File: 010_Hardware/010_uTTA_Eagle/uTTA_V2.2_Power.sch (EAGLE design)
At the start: 124 parts, among them IC1 MCP14E09, IC101 78L05SMD, IC102 7905ACM, IC103 LM393D, IC105 LT1167, IC2 SFH6156, IC3 SFH6156, IC4 SFH6156, J102 PIN23866A.68, J103 PIN23866A.68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

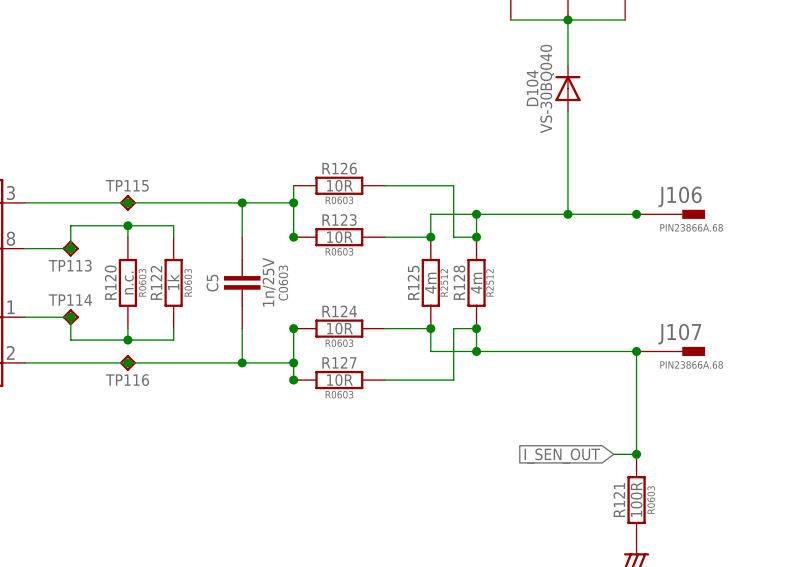
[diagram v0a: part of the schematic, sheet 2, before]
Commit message: Update to uTTA Version 2.2
Full update of both PCBs to HW Version 2.2:
Removed spare FLASH Memory
Adjusted Position of LEDs and Buttons
Cleanup of layout
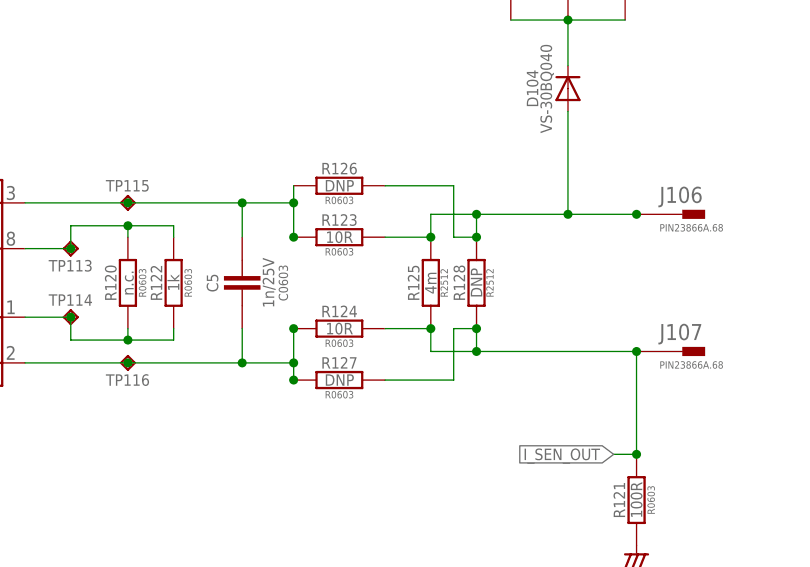
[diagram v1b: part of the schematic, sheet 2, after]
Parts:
- R126, R127: value 10R -> DNP
- R128: value 4m -> DNP
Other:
- note added: "2mv/A Ptot @ 15A: 0.9W"
- note added: "AV = 50V/V 15A -> 3.0V ~4.02mA/digit"
- note added: "AV = 50V/V 15A -> 3.0V ~4.02mA/digit tau = 2.2µs fc = 72.343kHz"
- note removed: "2mv/A Ptot @ 30A: 1.8W"
- note removed: "AV = 50V/V 30A -> 1.5V ~12.2mA/digit"
- note removed: "AV = 50V/V 30A -> 1.5V ~12.2mA/digit tau = 2.2µs fc = 72.343kHz"
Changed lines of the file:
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@@
 <schematic xreflabel="%F%N/%S.%C%R" xrefpart="/%S.%C%R">
 <attributes>
-<attribute name="VERSION" value="V1.0"/>
+<attribute name="VERSION" value="2.2"/>
 </attributes>
 <variantdefs>
@@
 </classes>
 <parts>
-<part name="R127" library="A_Resistor" deviceset="R-EU_" device="R0603" value="10R"/>
+<part name="R127" library="A_Resistor" deviceset="R-EU_" device="R0603" value="DNP"/>
 <part name="R124" library="A_Resistor" deviceset="R-EU_" device="R0603" value="10R"/>
 <part name="R123" library="A_Resistor" deviceset="R-EU_" device="R0603" value="10R"/>
-<part name="R126" library="A_Resistor" deviceset="R-EU_" device="R0603" value="10R"/>
+<part name="R126" library="A_Resistor" deviceset="R-EU_" device="R0603" value="DNP"/>
 <part name="R118" library="A_Resistor" deviceset="R-EU_" device="R0603" value="10R">
 <attribute name="PACKAGE" value="R0603"/>
@@
 <part name="D101" library="A_Dioden" deviceset="DIODE-" device="SOD123" value="1N4148"/>
 <part name="D102" library="A_Dioden" deviceset="DIODE-" device="SOD123" value="1N4148"/>
-<part name="R128" library="A_Shunts" deviceset="WSL2512" device="" value="4m"/>
+<part name="R128" library="A_Shunts" deviceset="WSL2512" device="" value="DNP"/>
 <part name="R125" library="A_Shunts" deviceset="WSL2512" device="" value="4m"/>
 <part name="C101" library="A_Kondensatoren" deviceset="CPOL-EU" device="D" value="47µF/25V"/>
@@
 <text x="144.78" y="152.4" size="2.1844" layer="98">RDS,on ~3.3mR</text>
 <text x="208.28" y="68.58" size="2.1844" layer="98">2mv/A
-Ptot @ 30A: 1.8W</text>
+Ptot @ 15A: 0.9W</text>
 <text x="120.015" y="48.26" size="1.4224" layer="98">AV = 50V/V
-30A -&gt; 1.5V
-~12.2mA/digit</text>
+15A -&gt; 3.0V
+~4.02mA/digit</text>
 <text x="116.205" y="85.725" size="1.27" layer="98">Replaceable with INA128</text>
 <text x="40.64" y="115.57" size="1.27" layer="98">UF=1.7V @ 16mA</text>
 <text x="97.155" y="53.34" size="1.4224" layer="98">AV = 50V/V
-30A -&gt; 1.5V
-~12.2mA/digit
+15A -&gt; 3.0V
+~4.02mA/digit
 tau = 2.2µs
 fc = 72.343kHz</text>

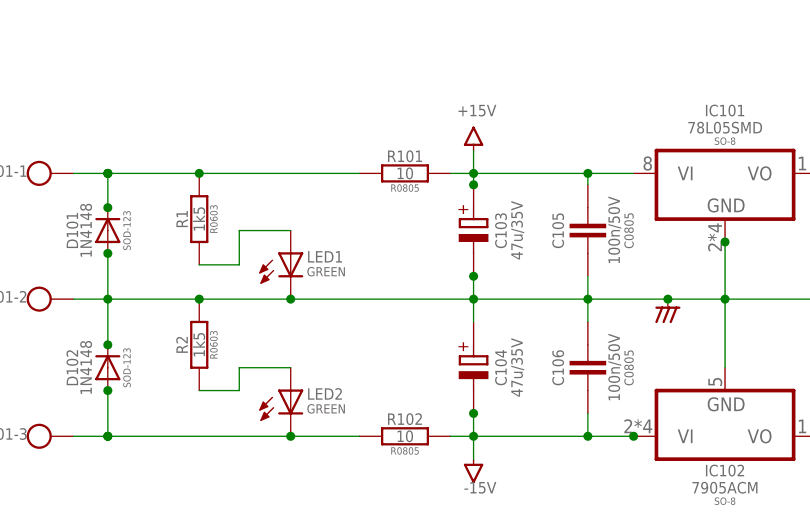
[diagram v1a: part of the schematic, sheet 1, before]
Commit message: changed resistor values
Changed Values of R101 and R102 to 0 Ohm
Changed value of R108 from 100 Ohm to 240 Ohm (to reduce optocoupler LED current)
Changed value of R110 from 220 Ohm to 470 Ohm (to reduce LED current)
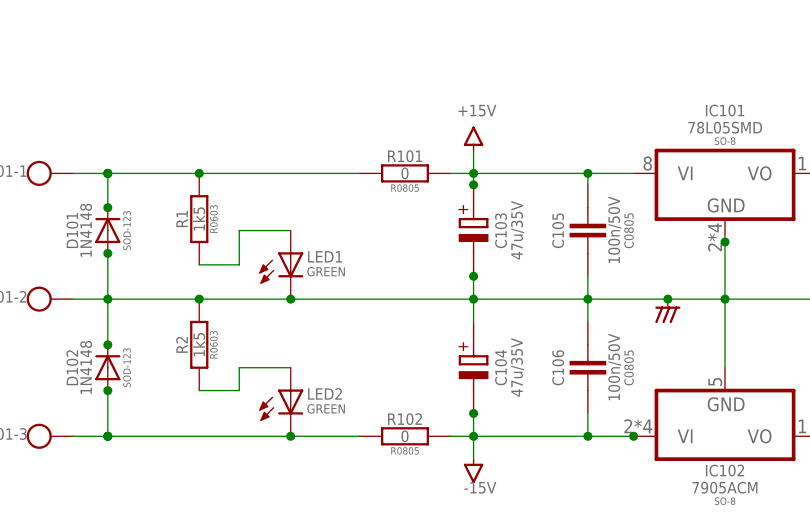
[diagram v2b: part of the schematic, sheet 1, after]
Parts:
- R101, R102: value 10 -> 0
- R108: value 100R -> 240R
- R110: value 270R -> 470R
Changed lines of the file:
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@@
 <schematic xreflabel="%F%N/%S.%C%R" xrefpart="/%S.%C%R">
 <attributes>
-<attribute name="VERSION" value="2.2"/>
+<attribute name="VERSION" value="2.5.3"/>
 </attributes>
 <variantdefs>
@@
 <attribute name="PACKAGE" value="R0603"/>
 </part>
-<part name="R101" library="A_Resistor" deviceset="R-EU_" device="R0805" value="10"/>
-<part name="R102" library="A_Resistor" deviceset="R-EU_" device="R0805" value="10"/>
+<part name="R101" library="A_Resistor" deviceset="R-EU_" device="R0805" value="0"/>
+<part name="R102" library="A_Resistor" deviceset="R-EU_" device="R0805" value="0"/>
 <part name="V40" library="supply" deviceset="+15V" device=""/>
 <part name="V41" library="supply" deviceset="-15V" device=""/>
@@
 <part name="R104" library="A_Resistor" deviceset="R-EU_" device="R0603" value="22k"/>
 <part name="AGND22" library="supply" deviceset="AGND_" device=""/>
-<part name="R108" library="A_Resistor" deviceset="R-EU_" device="R0603" value="100R"/>
+<part name="R108" library="A_Resistor" deviceset="R-EU_" device="R0603" value="240R"/>
 <part name="V2" library="supply" deviceset="GND_ISO" device=""/>
 <part name="AGND23" library="supply" deviceset="AGND_" device=""/>
 <part name="T102" library="A_Transistoren" deviceset="PDTC*" device="" technology="143E"/>
-<part name="R110" library="A_Resistor" deviceset="R-EU_" device="R0603" value="270R"/>
+<part name="R110" library="A_Resistor" deviceset="R-EU_" device="R0603" value="470R"/>
 <part name="TP101" library="A_Testpoint" deviceset="TP" device="C90H30" value="TPC90H30"/>
 <part name="TP104" library="A_Testpoint" deviceset="TP" device="C90H30" value="TPC90H30"/>
